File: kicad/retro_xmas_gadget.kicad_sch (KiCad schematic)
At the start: 80 parts, among them J1 USB_C_Receptacle_USB2.0_16P, J2 SD_Card_Receptacle, J3 AudioJack3_SwitchTR, J4 Conn_01x18, J5 Conn_01x02, J6 Conn_01x03, J7 Conn_01x03, J8 Conn_01x07, Q1 UMH3N, Q2 SS8050, SW1 RESET, SW10 SELECT, SW11 START, SW12 A, SW13 B, SW2 BOOT, SW3 KH-SS12F23-G6, SW4 UP, SW5 DOWN, SW6 LEFT, SW7 RIGHT, SW8 MENU, SW9 OPTION, U1 CP2102N-Axx-xQFN28, U2 ESP32-S3-WROOM-1, U4 XC6210B332MR, U5 TP4056

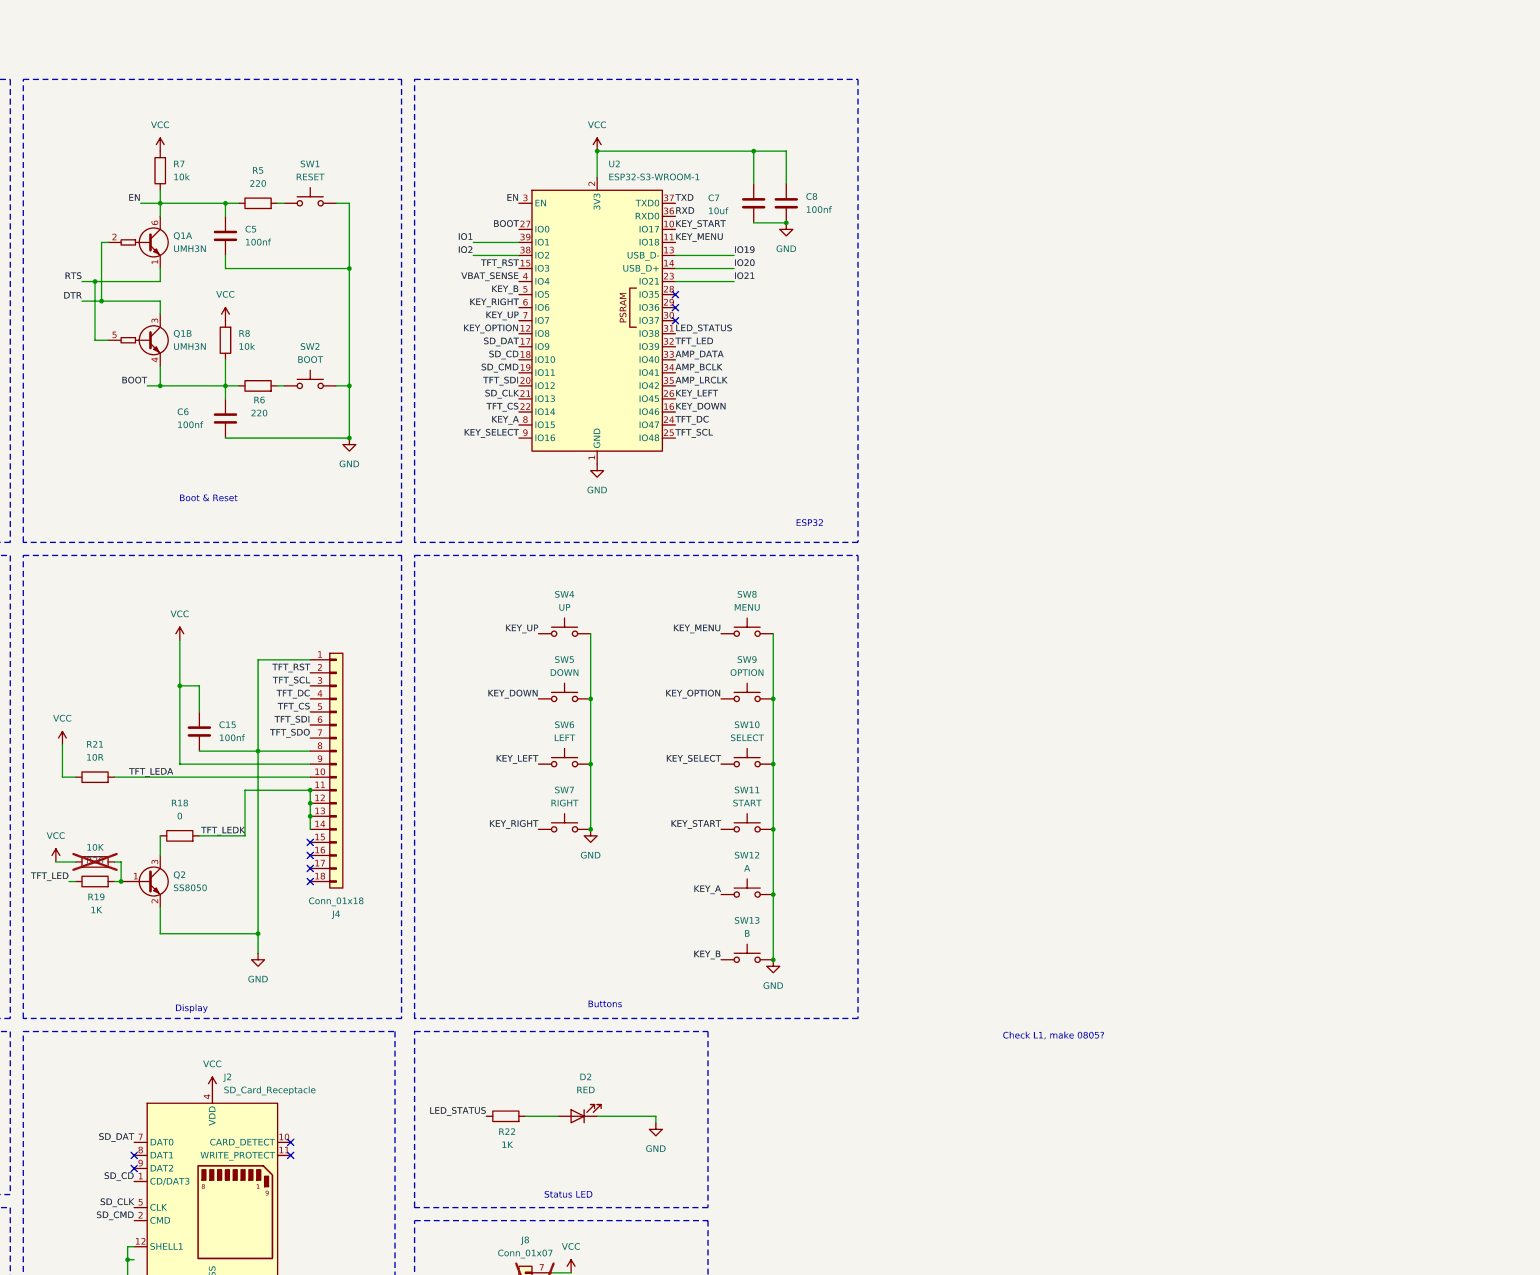
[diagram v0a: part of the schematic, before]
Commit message: Added ESP32-P4, added L,R,X and Y buttons
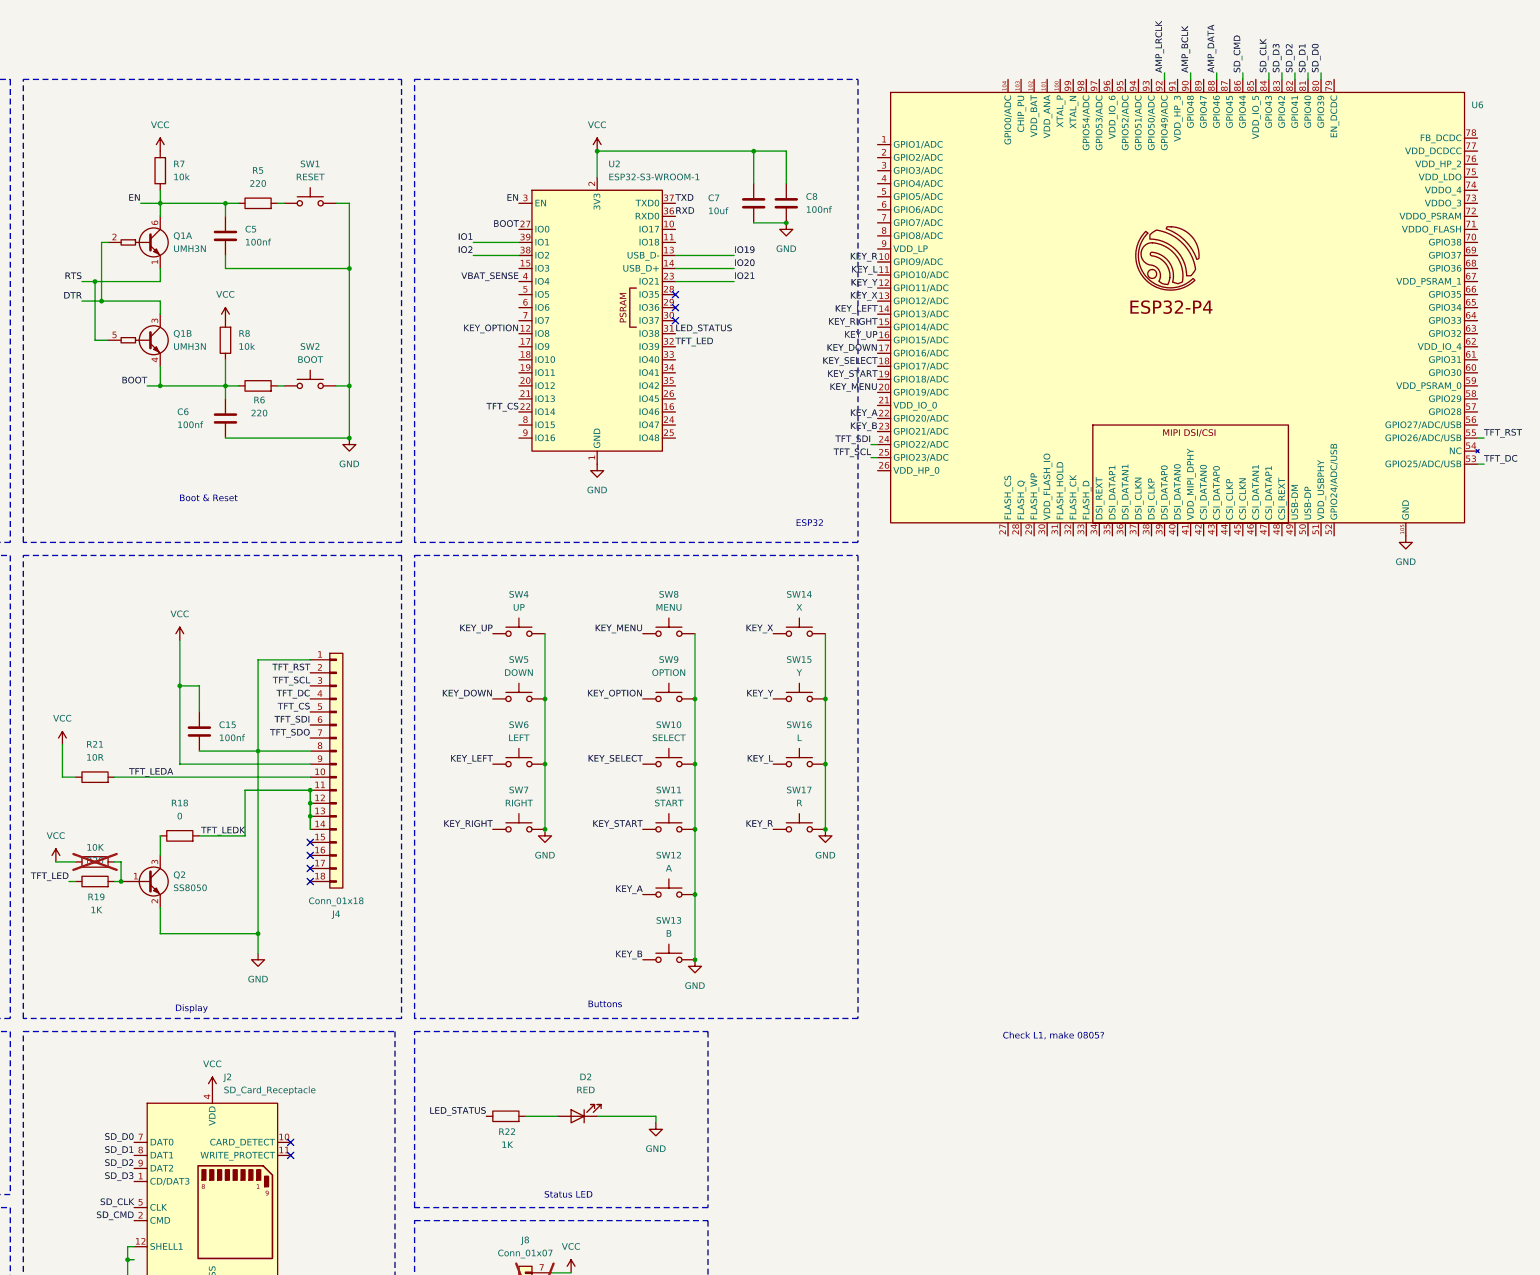
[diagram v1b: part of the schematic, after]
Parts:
- added SW14: X, Button_Switch_SMD:SW_SPST_SKQG_WithStem, symbol Switch:SW_Push
- added SW15: Y, Button_Switch_SMD:SW_SPST_SKQG_WithStem, symbol Switch:SW_Push
- added SW16: L, Button_Switch_SMD:SW_SPST_SKQG_WithStem, symbol Switch:SW_Push
- added SW17: R, Button_Switch_SMD:SW_SPST_SKQG_WithStem, symbol Switch:SW_Push
- added U6: ~, PCM_Espressif:ESP32-P4, symbol PCM_Espressif:ESP32-P4
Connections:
- net AMP_BCLK: now also U6.90 (GPIO48); no longer U2.34 (IO41)
- net AMP_DATA: now also U6.88 (GPIO46); no longer U2.33 (IO40)
- net AMP_LRCLK: now also U6.92 (GPIO49/ADC); no longer U2.35 (IO42)
- net GND: now also SW14.2, SW15.2, SW16.2, SW17.2, U6.105 (GND)
- net KEY_A: now also U6.22 (GPIO20/ADC); no longer U2.8 (IO15)
- net KEY_B: now also U6.23 (GPIO21/ADC); no longer U2.5 (IO5)
- net KEY_DOWN: now also U6.17 (GPIO16/ADC); no longer U2.16 (IO46)
- net KEY_LEFT: now also U6.14 (GPIO13/ADC); no longer U2.26 (IO45)
- net KEY_MENU: now also U6.20 (GPIO19/ADC); no longer U2.11 (IO18)
- net KEY_RIGHT: now also U6.15 (GPIO14/ADC); no longer U2.6 (IO6)
- net KEY_SELECT: now also U6.18 (GPIO17/ADC); no longer U2.9 (IO16)
- net KEY_START: now also U6.19 (GPIO18/ADC); no longer U2.10 (IO17)
- net KEY_UP: now also U6.16 (GPIO15/ADC); no longer U2.7 (IO7)
- net SD_CLK: now also U6.84 (GPIO43); no longer U2.21 (IO13)
- net SD_CMD: now also U6.86 (GPIO44); no longer U2.19 (IO11)
- net TFT_DC: now also U6.53 (GPIO25/ADC/USB); no longer U2.24 (IO47)
- net TFT_RST: now also U6.55 (GPIO26/ADC/USB); no longer U2.15 (IO3)
- net TFT_SCL: now also U6.25 (GPIO23/ADC); no longer U2.25 (IO48)
- net TFT_SDI: now also U6.24 (GPIO22/ADC); no longer U2.20 (IO12)
- net SD_D1: now reaches J2.8 (DAT1)
- net SD_D1: now also U6.81 (GPIO40)
- net SD_D2: now reaches J2.9 (DAT2)
- net SD_D2: now also U6.82 (GPIO41)
- net SD_CD: no longer names the net of U2.18 (IO10)
- net SD_CD: no longer J2.1 (CD/DAT3)
- net SD_DAT: no longer names the net of U2.17 (IO9)
- net SD_DAT: no longer J2.7 (DAT0)
- new net KEY_L: SW16.1, U6.11 (GPIO10/ADC)
- new net KEY_R: SW17.1, U6.10 (GPIO9/ADC)
- new net KEY_X: SW14.1, U6.13 (GPIO12/ADC)
- new net KEY_Y: SW15.1, U6.12 (GPIO11/ADC)
- new net SD_D0: J2.7 (DAT0), U6.80 (GPIO39)
- new net SD_D3: J2.1 (CD/DAT3), U6.83 (GPIO42)
- no-connect marks 33 -> 31
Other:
- moved on the sheet: SW10, SW11, SW12, SW13, SW4, SW5, SW6, SW7, SW8, SW9
